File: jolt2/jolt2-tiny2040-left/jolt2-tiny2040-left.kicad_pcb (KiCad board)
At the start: 2 copper layers, 151 x 98 mm, 34 parts, among them J1 RJ45, J10 Conn_01x02_Pin, J11 Conn_01x02_Pin, J12 Conn_01x02_Pin, J13 Conn_01x02_Pin, J14 Conn_01x02_Pin, J15 Conn_01x02_Pin, J16 Conn_01x02_Pin, J17 Conn_01x02_Pin, J18 Conn_01x02_Pin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

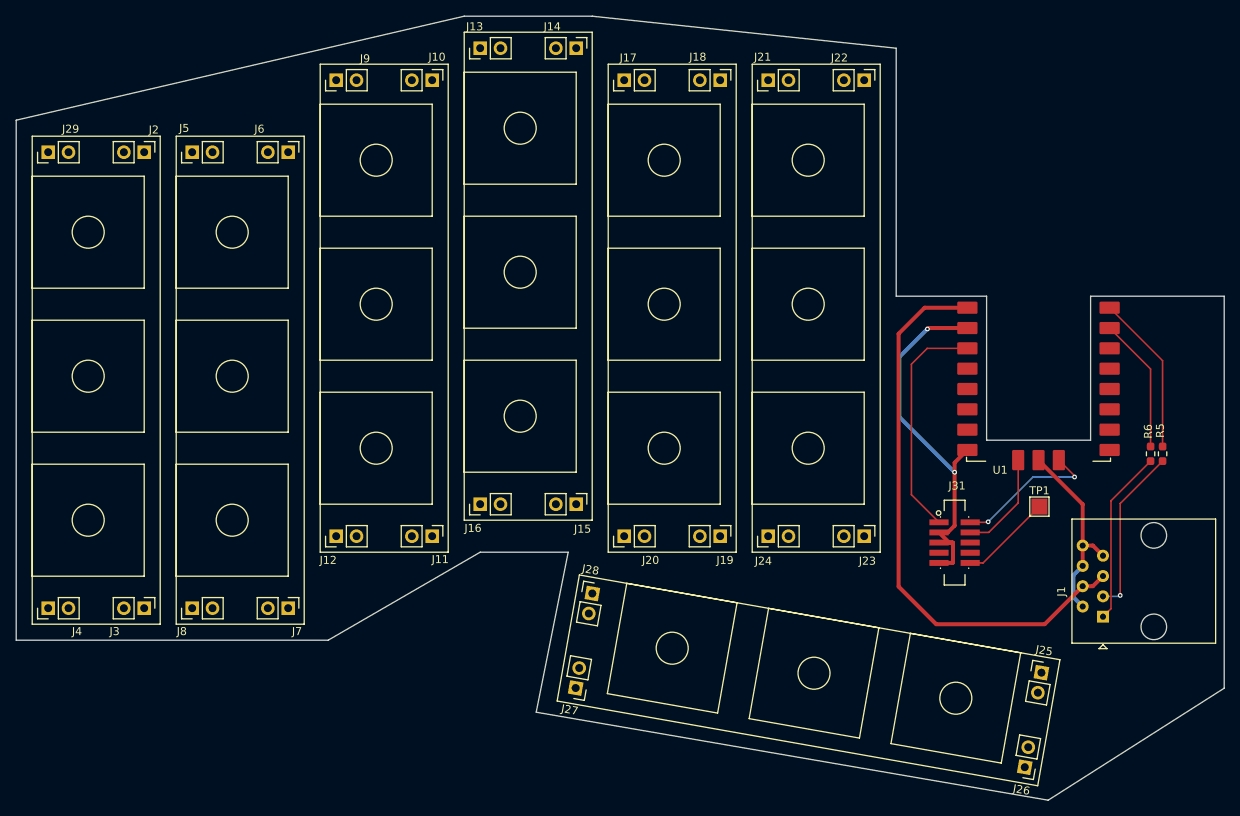
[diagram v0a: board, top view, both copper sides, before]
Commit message: jolt2-tiny204-left: Cleanup and route
Fix the designators for all of the pin headers.  This was mostly done
manually, naming them consistently for each component.

Perform manual routing.

This should be ready for REV A.
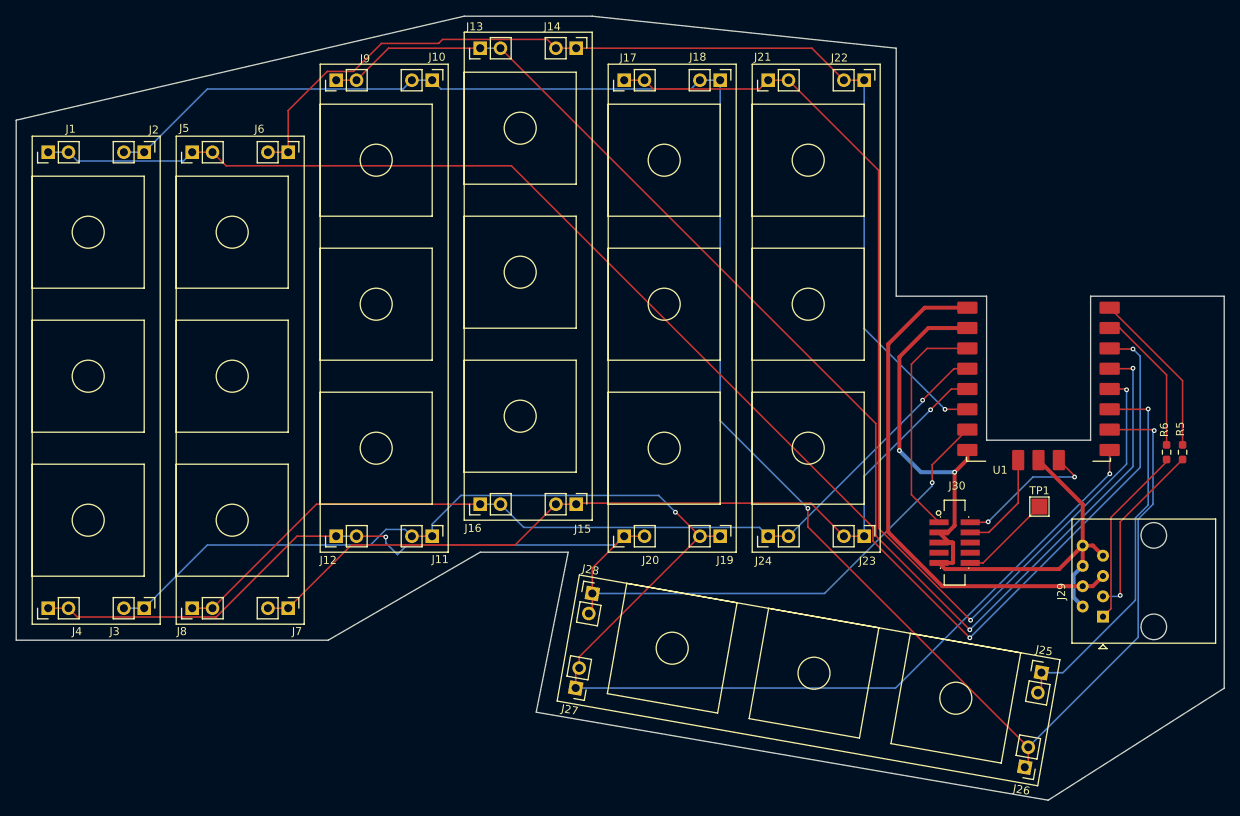
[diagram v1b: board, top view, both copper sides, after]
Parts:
- moved R5 2.51 mm to (182.8, 122.5)
- moved R6 2.01 mm to (180.8, 122.5)
- renumbered J29 to J1, J1 to J29, J31 to J30
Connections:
- J1 pad 1: /ROW-C -> /COL-A
- J1 pad 2: /ROW-C -> /COL-A
- J10 pad 1: /COL-B -> /ROW-A
- J10 pad 2: /COL-B -> /ROW-A
- J11 pad 1: /ROW-A -> /ROW-B
- J11 pad 2: /ROW-A -> /ROW-B
- J12 pad 1: /ROW-B -> /ROW-C
- J12 pad 2: /ROW-B -> /ROW-C
- J13 pad 1: /ROW-C -> /COL-B
- J13 pad 2: /ROW-C -> /COL-B
- J14 pad 1: /COL-B -> /ROW-D
- J14 pad 2: /COL-B -> /ROW-D
- J15 pad 1: /ROW-D -> /ROW-E
- J15 pad 2: /ROW-D -> /ROW-E
- J16 pad 1: /ROW-E -> /ROW-F
- J16 pad 2: /ROW-E -> /ROW-F
- J17 pad 1: /ROW-F -> /COL-C
- J17 pad 2: /ROW-F -> /COL-C
- J18 pad 1: /COL-C -> /ROW-A
- J18 pad 2: /COL-C -> /ROW-A
- J19 pad 1: /ROW-A -> /ROW-B
- J19 pad 2: /ROW-A -> /ROW-B
- J2 pad 1: /COL-A -> /ROW-A
- J2 pad 2: /COL-A -> /ROW-A
- J20 pad 1: /ROW-B -> /ROW-C
- J20 pad 2: /ROW-B -> /ROW-C
- J21 pad 1: /ROW-C -> /COL-C
- J21 pad 2: /ROW-C -> /COL-C
- J22 pad 1: /COL-C -> /ROW-D
- J22 pad 2: /COL-C -> /ROW-D
- J23 pad 1: /ROW-D -> /ROW-E
- J23 pad 2: /ROW-D -> /ROW-E
- J24 pad 1: /ROW-E -> /ROW-F
- J24 pad 2: /ROW-E -> /ROW-F
- J25 pad 1: /ROW-F -> /COL-D
- J25 pad 2: /ROW-F -> /COL-D
- J26 pad 1: /COL-D -> /ROW-A
- J26 pad 2: /COL-D -> /ROW-A
- J27 pad 1: /ROW-A -> /ROW-B
- J27 pad 2: /ROW-A -> /ROW-B
- J28 pad 1: /ROW-B -> /ROW-C
- J28 pad 2: /ROW-B -> /ROW-C
- J3 pad 1: /ROW-A -> /ROW-B
- J3 pad 2: /ROW-A -> /ROW-B
- J4 pad 1: /ROW-B -> /ROW-C
- J4 pad 2: /ROW-B -> /ROW-C
- J5 pad 1: /ROW-C -> /COL-A
- J5 pad 2: /ROW-C -> /COL-A
- J6 pad 1: /COL-A -> /ROW-D
- J6 pad 2: /COL-A -> /ROW-D
- J7 pad 1: /ROW-D -> /ROW-E
- J7 pad 2: /ROW-D -> /ROW-E
- J8 pad 1: /ROW-E -> /ROW-F
- J8 pad 2: /ROW-E -> /ROW-F
- J9 pad 1: /ROW-F -> /COL-B
- J9 pad 2: /ROW-F -> /COL-B
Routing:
- net /ROW-A: track 0.00 -> 232.9 mm, vias 0 -> 2
- net /COL-A: track 0.00 -> 190.5 mm, vias 0 -> 2
- net /ROW-B: track 0.00 -> 190.3 mm, vias 0 -> 2
- net /COL-B: track 0.00 -> 163.3 mm, vias 0 -> 2
- net /ROW-C: track 0.00 -> 149.9 mm, vias 0 -> 2
- net /COL-C: track 0.00 -> 137.4 mm, vias 0 -> 2
- net /ROW-D: track 0.00 -> 133.7 mm, vias 0 -> 1
- net /ROW-F: track 0.00 -> 112.8 mm, vias 0 -> 1
- net /ROW-E: track 0.00 -> 106.6 mm, vias 0 -> 1
- net /COL-D: track 0.00 -> 47.6 mm, vias 0 -> 1
- net GND: track 72.5 -> 94.5 mm
- net VBUS: track 71.5 -> 65.5 mm
- net Net-(R6-Pad1): track 16.9 -> 18.3 mm
- net SERTX: track 21.2 -> 22.4 mm
- net SERRX: track 21.9 -> 22.9 mm
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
